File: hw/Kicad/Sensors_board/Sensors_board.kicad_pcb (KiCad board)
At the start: 2 copper layers, 70 x 100 mm, 17 parts, among them J1 SENSORES_LINEA, U1 CNY70, U2 CNY70, U3 CNY70, U4 CNY70, U5 CNY70, U6 CNY70, U7 4053

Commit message: BOM modified
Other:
- board text added: "Cyclops-project"
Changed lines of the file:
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@@
     (links 46)
     (no_connects 0)
-    (area 91.424999 52.424999 161.575001 152.575001)
+    (area 91.424999 49.05 174.492857 160.700001)
     (thickness 1.6)
-    (drawings 31)
+    (drawings 32)
     (tracks 189)
     (zones 0)
@@
     )
   )
+  (gr_text Cyclops-project (at 135.7 101.6 90) (layer F.SilkS)
+    (effects (font (size 3.5 3.5) (thickness 0.7)))
+  )
   (dimension 13 (width 0.3) (layer Dwgs.User)
     (gr_text 13mm (at 133 159.35) (layer Dwgs.User)
@@
     (arrow2b (pts (xy 126.5 158) (xy 125.373496 158.586421)))
   )
-  (gr_text www.lnrc.es (at 117.25 98.5 270) (layer F.SilkS)
+  (gr_text www.lnrc.es (at 117.8 100.9 270) (layer F.SilkS)
     (effects (font (size 4 4) (thickness 0.7)))
   )

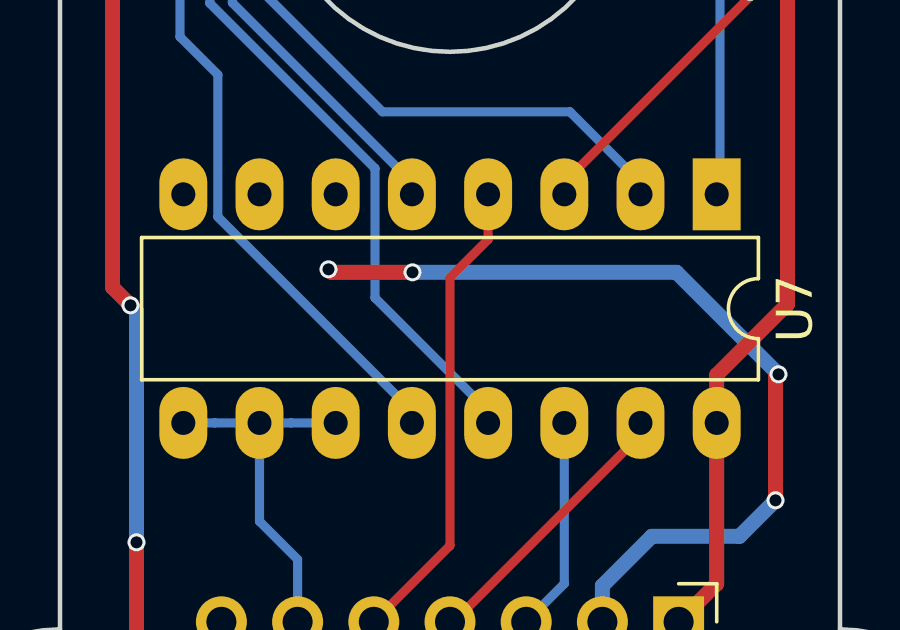
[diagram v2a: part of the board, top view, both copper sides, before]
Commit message: PCB silk modified
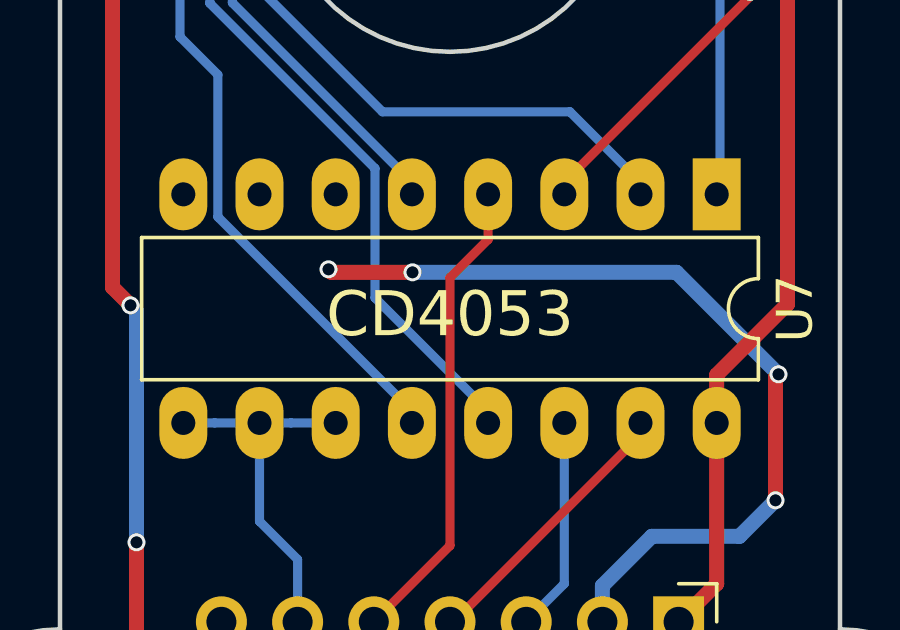
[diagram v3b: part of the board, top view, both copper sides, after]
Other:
- board text added: "CD4053"
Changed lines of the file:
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@@
     (area 91.424999 49.05 174.492857 160.700001)
     (thickness 1.6)
-    (drawings 32)
+    (drawings 33)
     (tracks 189)
     (zones 0)
@@
     )
   )
+  (gr_text CD4053 (at 126.5 132) (layer F.SilkS)
+    (effects (font (size 1.5 1.5) (thickness 0.2)))
+  )
   (gr_text Cyclops-project (at 135.7 101.6 90) (layer F.SilkS)

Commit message: PCBs silkscreen updated
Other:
- board text added: "Designed by Resaj"
- board text removed: "RESAJ"
- board text removed: "www.lnrc.es"
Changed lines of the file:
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@@
-(kicad_pcb (version 4) (host pcbnew 4.0.6)
+(kicad_pcb (version 4) (host pcbnew 4.0.7)
   (general
     (links 46)
@@
     (area 91.424999 49.05 174.492857 160.700001)
     (thickness 1.6)
-    (drawings 33)
+    (drawings 32)
     (tracks 189)
     (zones 0)
@@
   (title_block
     (title "Sensors Board robot de carreras educativo")
-    (company "Liga Nacional de Robótica de Competición")
-    (comment 1 www.lnrc.es)
-    (comment 2 "Diseño de Rubén Espino San José")
+    (comment 1 "Diseño de Rubén Espino San José")
   )
   (layers
@@
       (psa4output false)
       (plotreference true)
-      (plotvalue true)
+      (plotvalue false)
       (plotinvisibletext false)
       (padsonsilk false)
@@
     (arrow2b (pts (xy 126.5 158) (xy 125.373496 158.586421)))
   )
-  (gr_text www.lnrc.es (at 117.8 100.9 270) (layer F.SilkS)
-    (effects (font (size 4 4) (thickness 0.7)))
-  )
-  (gr_text RESAJ (at 126.5 139) (layer B.SilkS)
-    (effects (font (size 2.5 2.5) (thickness 0.3)) (justify mirror))
+  (gr_text "Designed by Resaj" (at 117.7 100.9 270) (layer F.SilkS)
+    (effects (font (size 3 3) (thickness 0.6)))
   )
   (gr_line (start 126.5 52.5) (end 126.5 152.5) (angle 90) (layer Dwgs.User) (width 0.2))

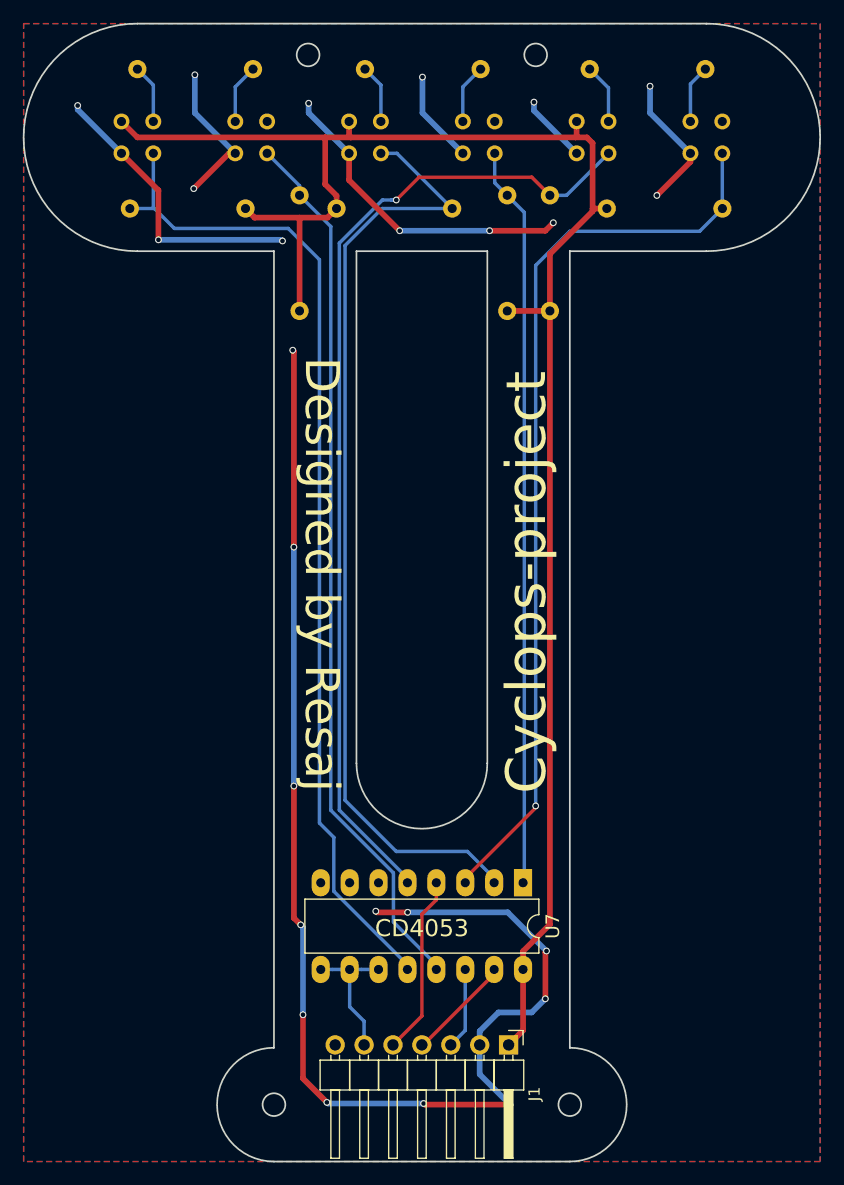
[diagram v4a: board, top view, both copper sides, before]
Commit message: PCBs adapted with Kicad libraries models
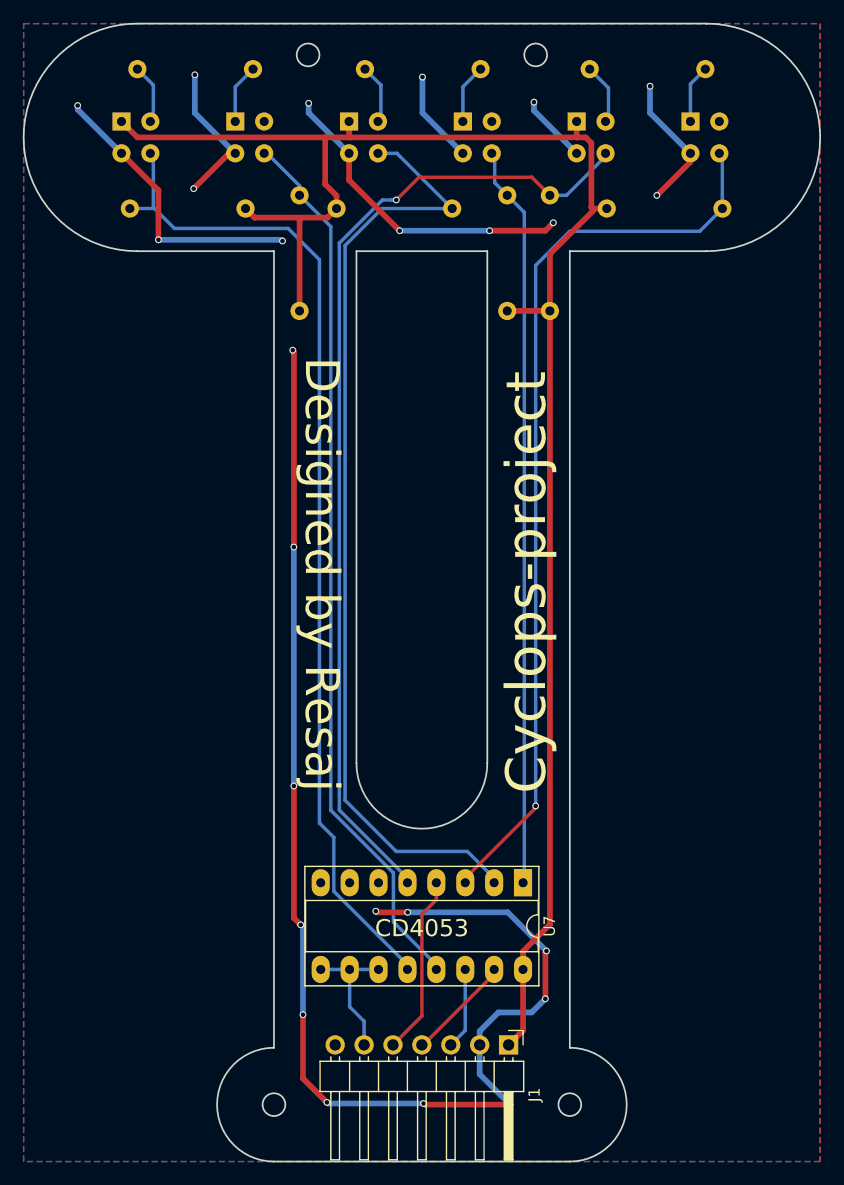
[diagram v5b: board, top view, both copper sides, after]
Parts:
- J1: footprint Pin_Headers:Pin_Header_Angled_1x07_Pitch2.54mm -> Sensors_board:PinHeader_1x07_P2.54mm_Horizontal
- R1, R2, R3, R4, R5, R6, R7, R8, R9: footprint Resistors_THT:R_Axial_DIN0207_L6.3mm_D2.5mm_P10.16mm_Horizontal -> Sensors_board:R_Axial_DIN0207_L6.3mm_D2.5mm_P10.16mm_Horizontal
- U1, U2, U3, U4, U5, U6: footprint Sensors_board:CNY70 -> Sensors_board:Vishay_CNY70
- U7: footprint Housings_DIP:DIP-16_W7.62mm_LongPads -> Sensors_board:DIP-16_W7.62mm_Socket_LongPads
- moved U1 1.98 mm to (100.1, 61.1)
- moved U2 1.98 mm to (110.1, 61.1)
- moved U3 1.98 mm to (120.1, 61.1)
- moved U4 1.98 mm to (130.1, 61.1)
- moved U5 1.98 mm to (140.1, 61.1)
- moved U6 1.98 mm to (150.1, 61.1)
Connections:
- J1 pad 7: Net-(J1-Pad7) -> (no net)
